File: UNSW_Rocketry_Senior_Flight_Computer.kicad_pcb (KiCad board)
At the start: 2 copper layers, 14 parts, among them U1 STM32L452RETx, U2 MS5611-01BA, U3 MS5611-01BA, U4 LIS3DH

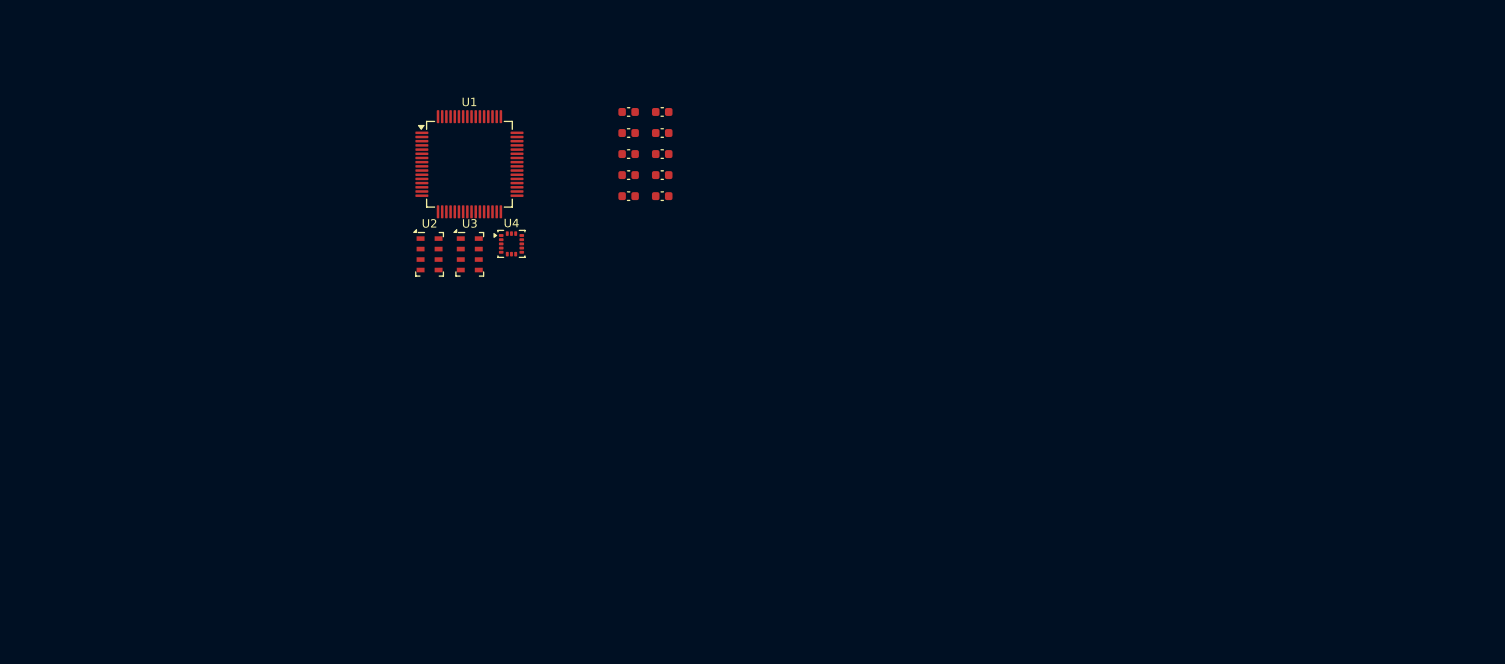
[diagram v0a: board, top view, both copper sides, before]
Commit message: feat: BCB Start ( power & pyro done)
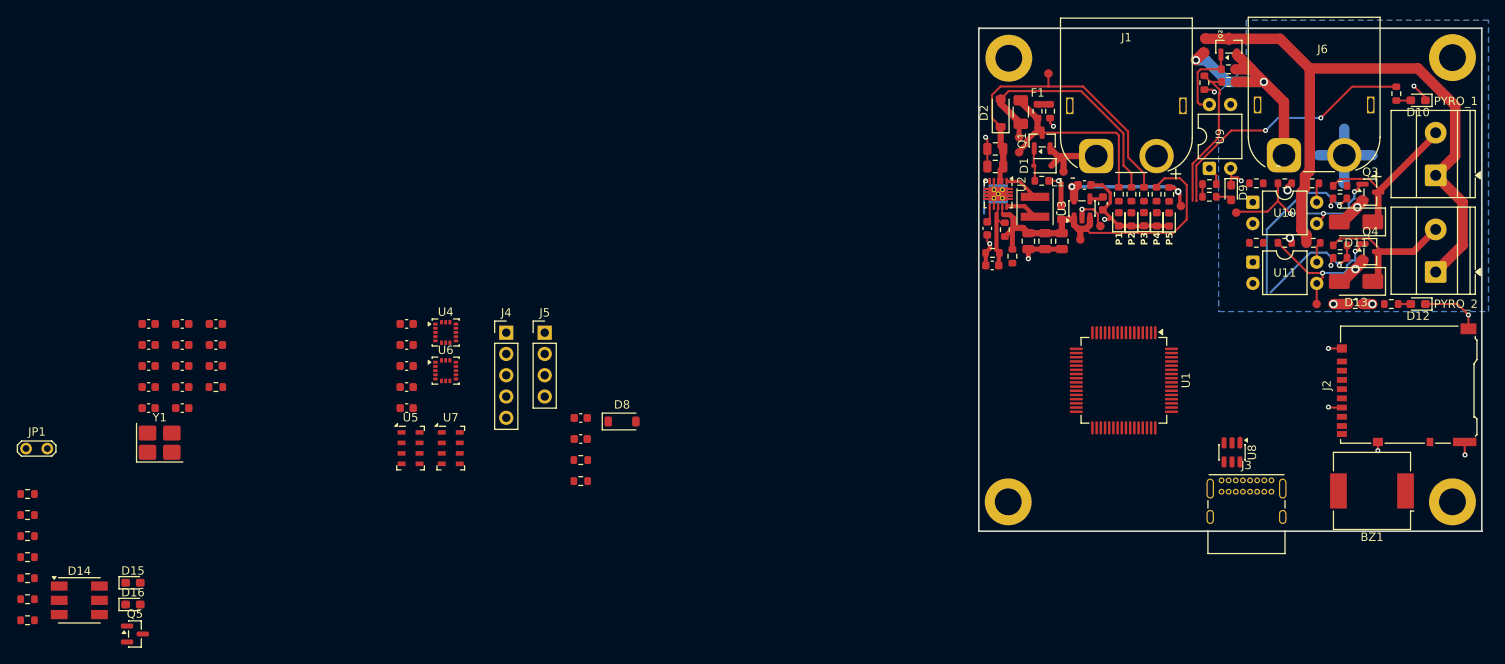
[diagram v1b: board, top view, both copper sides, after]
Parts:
- added BZ1: Buzzer, Buzzer_Beeper:Buzzer_CUI_CPT-9019S-SMT, F.Cu at (207.4, 114.7)
- added C11: 0.1uF, PCM_SparkFun-Capacitor:C_0603_1608Metric, F.Cu at (69.5, 94.8)
- added C12: 4.7uF, PCM_SparkFun-Capacitor:C_0603_1608Metric, F.Cu at (69.5, 97.3)
- added C13: 0.1uF, PCM_SparkFun-Capacitor:C_0603_1608Metric, F.Cu at (69.5, 99.8)
- added C14: 10uF, PCM_SparkFun-Capacitor:C_0805_2012Metric, F.Cu at (162.5, 73.9)
- added C15: 10uF, PCM_SparkFun-Capacitor:C_0805_2012Metric, F.Cu at (162.5, 76.0)
- added C16: 22uF, PCM_SparkFun-Capacitor:C_0805_2012Metric, F.Cu at (166.4, 84.9)
- added C17: 0.1uF, PCM_SparkFun-Capacitor:C_0603_1608Metric, F.Cu at (161.5, 83.4)
- added C18: 22uF, PCM_SparkFun-Capacitor:C_0805_2012Metric, F.Cu at (168.4, 84.9)
- added C19: 10pF, PCM_SparkFun-Capacitor:C_0603_1608Metric, F.Cu at (162.1, 87.8)
- added C20: 22uF, PCM_SparkFun-Capacitor:C_0805_2012Metric, F.Cu at (170.4, 84.9)
- added C21: 1.0uF, PCM_SparkFun-Capacitor:C_0603_1608Metric, F.Cu at (170.3, 81.5)
- added C22: 1.0uF, PCM_SparkFun-Capacitor:C_0603_1608Metric, F.Cu at (173.1, 78.2)
- added C23: 10nF, PCM_SparkFun-Capacitor:C_0603_1608Metric, F.Cu at (175.3, 80.4)
- added C24: 0.1uF, PCM_SparkFun-Capacitor:C_0603_1608Metric, F.Cu at (92.2, 94.8)
- added C25: 0.1uF, PCM_SparkFun-Capacitor:C_0603_1608Metric, F.Cu at (92.2, 97.3)
- added C26: 0.1uF, PCM_SparkFun-Capacitor:C_0603_1608Metric, F.Cu at (92.2, 99.8)
- added C27: 0.1uF, PCM_SparkFun-Capacitor:C_0603_1608Metric, F.Cu at (92.2, 102.3)
- added C28: 0.1uF, PCM_SparkFun-Capacitor:C_0603_1608Metric, F.Cu at (92.2, 104.8)
- added C29: 1.0uF, PCM_SparkFun-Capacitor:C_0603_1608Metric, F.Cu at (113.0, 106.0)
- added C30: 0.1uF, PCM_SparkFun-Capacitor:C_0603_1608Metric, F.Cu at (113.0, 108.5)
- added D1: 5.1V, Diode_SMD:D_SOD-323, F.Cu at (168.1, 75.9)
- added D10: LED_YELLOW, LED_SMD:LED_0603_1608Metric_Pad1.05x0.95mm_HandSolder, F.Cu at (212.9, 68.1)
- added D11: SMAJ15A, Diode_SMD:D_SMA, F.Cu at (205.5, 82.6)
- added D12: LED_YELLOW, LED_SMD:LED_0603_1608Metric_Pad1.05x0.95mm_HandSolder, F.Cu at (212.9, 92.4)
- added D13: SMAJ15A, Diode_SMD:D_SMA, F.Cu at (205.5, 89.7)
- added D14: LED_RGB, LED_SMD:LED_RGB_5050-6, F.Cu at (53.2, 127.8)
- added D15: LED_RED, LED_SMD:LED_0603_1608Metric_Pad1.05x0.95mm_HandSolder, F.Cu at (59.6, 125.7)
- added D16: LED_GREEN, LED_SMD:LED_0603_1608Metric_Pad1.05x0.95mm_HandSolder, F.Cu at (59.6, 128.2)
- added D2: B5819W, Diode_SMD:D_SOD-123, F.Cu at (163.1, 69.6)
- added D3: Green, LED_SMD:LED_0603_1608Metric, F.Cu at (177.2, 82.3)
- added D4: Green, LED_SMD:LED_0603_1608Metric, F.Cu at (180.2, 82.3)
- added D5: Green, LED_SMD:LED_0603_1608Metric, F.Cu at (178.7, 82.3)
- added D6: Green, LED_SMD:LED_0603_1608Metric, F.Cu at (181.7, 82.3)
- added D7: Green, LED_SMD:LED_0603_1608Metric, F.Cu at (183.2, 82.3)
- added D8: B5819W, Diode_SMD:D_SOD-123, F.Cu at (117.9, 106.4)
- added D9: LED_RED, LED_SMD:LED_0603_1608Metric_Pad1.05x0.95mm_HandSolder, F.Cu at (190.6, 79.1)
- added F1: 1A, Fuse:Fuse_1206_3216Metric, F.Cu at (165.5, 69.5)
- added H1: MountingHole, MountingHole:MountingHole_3.2mm_M3_DIN965_Pad, F.Cu at (164.1, 63.1)
- added H2: MountingHole, MountingHole:MountingHole_3.2mm_M3_DIN965_Pad, F.Cu at (217.0, 63.0)
- added H3: MountingHole, MountingHole:MountingHole_3.2mm_M3_DIN965_Pad, F.Cu at (217.0, 116.0)
- added H4: MountingHole, MountingHole:MountingHole_3.2mm_M3_DIN965_Pad, F.Cu at (164.0, 116.0)
- added J1: BATT_XT60, Connector_AMASS:AMASS_XT60PW-M_1x02_P7.20mm_Horizontal, F.Cu at (174.5, 74.8)
- added J2: Micro_SD_Card_Det1, Connector_Card:microSD_HC_Hirose_DM3AT-SF-PEJM5, F.Cu at (211.5, 102.0)
- added J3: USB_C_Receptacle_USB2.0_16P, Connector_USB:USB_C_Receptacle_GCT_USB4085, F.Cu at (189.4, 113.4)
- added J4: SWD, Connector_PinHeader_2.54mm:PinHeader_1x05_P2.54mm_Vertical, F.Cu at (104.1, 95.8)
- added J5: Conn_01x04, Connector_PinHeader_2.54mm:PinHeader_1x04_P2.54mm_Vertical, F.Cu at (108.7, 95.8)
- added J6: PYRO_XT60, Connector_AMASS:AMASS_XT60PW-M_1x02_P7.20mm_Horizontal, F.Cu at (196.9, 74.7)
- added JP1: RESET_JMP, TestPoint:TestPoint_2Pads_Pitch2.54mm_Drill0.8mm, F.Cu at (46.8, 109.6)
- added L1: 1µH, Inductor_SMD:L_Coilcraft_XxL4020, F.Cu at (167.2, 80.8)
- added PYRO_1: J_PYRO1, TerminalBlock_Phoenix:TerminalBlock_Phoenix_MKDS-1,5-2-5.08_1x02_P5.08mm_Horizontal, F.Cu at (215.0, 77.0)
- added PYRO_2: J_PYRO2, TerminalBlock_Phoenix:TerminalBlock_Phoenix_MKDS-1,5-2-5.08_1x02_P5.08mm_Horizontal, F.Cu at (215.0, 88.6)
- added Q1: DMG2301L, Package_TO_SOT_SMD:SOT-23, F.Cu at (168.1, 72.9)
- added Q2: AO3401A, Package_TO_SOT_SMD:SOT-23, F.Cu at (190.3, 61.7)
- added Q3: AO3400A, Package_TO_SOT_SMD:SOT-23, F.Cu at (207.2, 79.0)
- added Q4: AO3400A, Package_TO_SOT_SMD:SOT-23, F.Cu at (207.2, 86.2)
- added Q5: AO3400A, Package_TO_SOT_SMD:SOT-23, F.Cu at (59.8, 131.8)
- added R1: 10k, PCM_SparkFun-Resistor:R_0603_1608Metric, F.Cu at (69.5, 102.3)
- added R10: 4.7k, PCM_SparkFun-Resistor:R_0603_1608Metric, F.Cu at (178.7, 79.3)
- added R11: 1k, PCM_SparkFun-Resistor:R_0603_1608Metric, F.Cu at (181.7, 79.3)
- added R12: 1k, PCM_SparkFun-Resistor:R_0603_1608Metric, F.Cu at (183.2, 79.3)
- added R13: 5.1k, PCM_SparkFun-Resistor:R_0603_1608Metric, F.Cu at (113.0, 111.0)
- added R14: 5.1k, PCM_SparkFun-Resistor:R_0603_1608Metric, F.Cu at (113.0, 113.5)
- added R15: 10k, PCM_SparkFun-Resistor:R_0603_1608Metric, F.Cu at (190.3, 65.9)
- added R16: 3.3k, PCM_SparkFun-Resistor:R_0603_1608Metric, F.Cu at (187.4, 66.0)
- added R17: 0, PCM_SparkFun-Resistor:R_0603_1608Metric, F.Cu at (205.4, 92.4)
- added R18: 330, PCM_SparkFun-Resistor:R_0603_1608Metric, F.Cu at (188.0, 78.1)
- added R19: 1k, PCM_SparkFun-Resistor:R_0603_1608Metric, F.Cu at (188.0, 79.6)
- added R2: 620k, PCM_SparkFun-Resistor:R_0603_1608Metric, F.Cu at (163.6, 83.5)
- added R20: 330, PCM_SparkFun-Resistor:R_0603_1608Metric, F.Cu at (193.6, 78.0)
- added R21: 100k, PCM_SparkFun-Resistor:R_0603_1608Metric, F.Cu at (190.3, 64.4)
- added R22: 10k, PCM_SparkFun-Resistor:R_0603_1608Metric, F.Cu at (200.2, 78.0)
- added R23: 10k, PCM_SparkFun-Resistor:R_0603_1608Metric, F.Cu at (197.0, 78.0)
- added R24: 1k, PCM_SparkFun-Resistor:R_0603_1608Metric, F.Cu at (210.3, 67.3)
- added R25: 10k, PCM_SparkFun-Resistor:R_0603_1608Metric, F.Cu at (203.6, 78.3)
- added R26: 3.3k, PCM_SparkFun-Resistor:R_0603_1608Metric, F.Cu at (203.6, 79.8)
- added R27: 330, PCM_SparkFun-Resistor:R_0603_1608Metric, F.Cu at (193.6, 85.1)
- added R28: 10k, PCM_SparkFun-Resistor:R_0603_1608Metric, F.Cu at (200.4, 85.1)
- added R29: 10k, PCM_SparkFun-Resistor:R_0603_1608Metric, F.Cu at (197.0, 85.1)
- added R3: 100k, PCM_SparkFun-Resistor:R_0603_1608Metric, F.Cu at (164.5, 86.7)
- added R30: 1k, PCM_SparkFun-Resistor:R_0603_1608Metric, F.Cu at (209.7, 92.4)
- added R31: 10k, PCM_SparkFun-Resistor:R_0603_1608Metric, F.Cu at (203.6, 85.4)
- added R32: 3.3k, PCM_SparkFun-Resistor:R_0603_1608Metric, F.Cu at (203.6, 86.9)
- added R33: 100, PCM_SparkFun-Resistor:R_0603_1608Metric, F.Cu at (47.0, 115.1)
- added R34: 100, PCM_SparkFun-Resistor:R_0603_1608Metric, F.Cu at (47.0, 117.6)
- added R35: 100, PCM_SparkFun-Resistor:R_0603_1608Metric, F.Cu at (47.0, 120.1)
- added R36: 150, PCM_SparkFun-Resistor:R_0603_1608Metric, F.Cu at (47.0, 122.6)
- added R37: 10k, PCM_SparkFun-Resistor:R_0603_1608Metric, F.Cu at (47.0, 125.1)
- added R38: 1k, PCM_SparkFun-Resistor:R_0603_1608Metric, F.Cu at (47.0, 127.6)
- added R39: 1k, PCM_SparkFun-Resistor:R_0603_1608Metric, F.Cu at (47.0, 130.1)
- added R4: 100k, PCM_SparkFun-Resistor:R_0603_1608Metric, F.Cu at (162.1, 86.3)
- added R5: 100k, PCM_SparkFun-Resistor:R_0603_1608Metric, F.Cu at (168.0, 77.7)
- added R6: 10k, PCM_SparkFun-Resistor:R_0603_1608Metric, F.Cu at (169.0, 69.4)
- added R7: 33k, PCM_SparkFun-Resistor:R_0603_1608Metric, F.Cu at (167.5, 69.4)
- added R8: 4.7k, PCM_SparkFun-Resistor:R_0603_1608Metric, F.Cu at (177.2, 79.3)
- added R9: 4.7k, PCM_SparkFun-Resistor:R_0603_1608Metric, F.Cu at (180.2, 79.3)
- added TP1: 1.0mm, PCM_SparkFun-Connector:TestPoint-1.0mm, F.Cu at (170.6, 76.6)
- added TP10: 1.0mm, PCM_SparkFun-Connector:TestPoint-1.0mm, F.Cu at (191.2, 81.5)
- added TP12: 1.0mm, PCM_SparkFun-Connector:TestPoint-1.0mm, F.Cu at (200.8, 92.4)
- added TP2: 1.0mm, PCM_SparkFun-Connector:TestPoint-1.0mm, F.Cu at (172.6, 84.7)
- added TP3: 1.0mm, PCM_SparkFun-Connector:TestPoint-1.0mm, F.Cu at (165.3, 74.3)
- added TP4: 1.0mm, PCM_SparkFun-Connector:TestPoint-1.0mm, F.Cu at (175.0, 83.1)
- added TP5: 1.0mm, PCM_SparkFun-Connector:TestPoint-1.0mm, F.Cu at (184.6, 80.7)
- added TP6: 1.0mm, PCM_SparkFun-Connector:TestPoint-1.0mm, F.Cu at (165.3, 72.5)
- added TP7: 1.0mm, PCM_SparkFun-Connector:TestPoint-1.0mm, F.Cu at (168.8, 64.9)
- added TP8: 1.0mm, PCM_SparkFun-Connector:TestPoint-1.0mm, F.Cu at (187.4, 62.4)
- added TP9: 1.0mm, PCM_SparkFun-Connector:TestPoint-1.0mm, F.Cu at (187.5, 60.7)
- added U10: PC817, Package_DIP:DIP-4_W7.62mm, F.Cu at (193.2, 80.3)
- added U11: PC817, Package_DIP:DIP-4_W7.62mm, F.Cu at (193.2, 87.4)
- added U5: MS5611 #1, Package_LGA:LGA-8_3x5mm_P1.25mm, F.Cu at (92.7, 109.6)
- added U6: LIS3DH, Package_LGA:LGA-16_3x3mm_P0.5mm_LayoutBorder3x5y, F.Cu at (96.9, 100.3)
- added U7: MS5611 #2, Package_LGA:LGA-8_3x5mm_P1.25mm, F.Cu at (97.5, 109.6)
- added U8: USBLC6-2SC6, Package_TO_SOT_SMD:SOT-23-6, F.Cu at (190.7, 110.1)
- added U9: PC817, Package_DIP:DIP-4_W7.62mm, F.Cu at (188.0, 76.2)
- added Y1: 8MHz, Crystal:Crystal_SMD_3225-4Pin_3.2x2.5mm_HandSoldering, F.Cu at (62.8, 108.9)
- C1, C2: value 0.1uF -> 27pF
- C4: value 4.7uF -> 1.0uF
- C5: value 1.0uF -> 0.1uF
- C6: value 10nF -> 0.1uF
- C7: value 0.1uF -> 10nF
- U2: value MS5611-01BA -> TPS63060; footprint Package_LGA:LGA-8_3x5mm_P1.25mm -> Package_SON:Texas_S-PWSON-N10_ThermalVias
- U3: value MS5611-01BA -> SPX3819M5-L-3-3; footprint Package_LGA:LGA-8_3x5mm_P1.25mm -> Package_TO_SOT_SMD:SOT-23-5
- U4: value LIS3DH -> H3LIS331DL
- moved U1 82.2 mm to (177.8, 101.5), turned to -90 degrees
- moved U3 73.2 mm to (172.8, 81.0), turned to 90 degrees
- moved U2 68.2 mm to (162.8, 79.3), turned to -90 degrees
- moved C1 62.6 mm to (61.5, 94.8)
- moved C4 62.6 mm to (61.5, 102.3)
- moved C2 62.6 mm to (61.5, 97.3)
- moved C3 62.6 mm to (61.5, 99.8)
- moved C5 62.6 mm to (61.5, 104.8)
- moved C10 62.6 mm to (65.5, 104.8)
- moved C6 62.6 mm to (65.5, 94.8)
- moved C7 62.6 mm to (65.5, 97.3)
- moved C8 62.6 mm to (65.5, 99.8)
- moved C9 62.6 mm to (65.5, 102.3)
- moved U4 13.2 mm to (96.9, 95.8)
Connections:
- C1 pad 1: GND -> Net-(U1-PH1)
- C1 pad 2: +3.3V -> GND
- C10 pad 1: +3.3V -> GND
- C10 pad 2: GND -> +3.3V
- C2 pad 2: +3.3V -> Net-(U1-PH0)
- C3 pad 2: +3.3V -> NRST
- C6 pad 1: GND -> +3.3V
- C6 pad 2: +3.3V -> GND
- C8 pad 1: +3.3V -> GND
- C8 pad 2: GND -> +3.3V
- C9 pad 1: GND -> +3.3V
- C9 pad 2: +3.3V -> GND
- U1 pad 10: unconnected-(U1-PC2-Pad10) -> INT2_LIS3DH
- U1 pad 11: unconnected-(U1-PC3-Pad11) -> SD_CD
- U1 pad 14: unconnected-(U1-PA0-Pad14) -> PYRO1_CONT
- U1 pad 15: unconnected-(U1-PA1-Pad15) -> PYRO2_CONT
- U1 pad 16: unconnected-(U1-PA2-Pad16) -> UART_TX
- U1 pad 17: unconnected-(U1-PA3-Pad17) -> UART_RX
- U1 pad 20: unconnected-(U1-PA4-Pad20) -> PYRO_BATT_SENSE
- U1 pad 21: unconnected-(U1-PA5-Pad21) -> SPI1_SCK
- U1 pad 22: unconnected-(U1-PA6-Pad22) -> SPI1_MISO
- U1 pad 23: unconnected-(U1-PA7-Pad23) -> SPI1_MOSI
- U1 pad 24: unconnected-(U1-PC4-Pad24) -> VBAT_SENSE
- U1 pad 26: unconnected-(U1-PB0-Pad26) -> CS_H3LIS
- U1 pad 27: unconnected-(U1-PB1-Pad27) -> CS_LIS3DH
- U1 pad 28: unconnected-(U1-PB2-Pad28) -> CS_MS5611_1
- U1 pad 29: unconnected-(U1-PB10-Pad29) -> PYRO1_CONT_LED
- U1 pad 30: unconnected-(U1-PB11-Pad30) -> PYRO2_CONT_LED
- U1 pad 33: unconnected-(U1-PB12-Pad33) -> CS_MS5611_2
- U1 pad 34: unconnected-(U1-PB13-Pad34) -> PYRO_ARM
- U1 pad 35: unconnected-(U1-PB14-Pad35) -> PYRO1_GATE
- U1 pad 36: unconnected-(U1-PB15-Pad36) -> PYRO2_GATE
- U1 pad 39: unconnected-(U1-PC8-Pad39) -> SDMMC_D0
- U1 pad 40: unconnected-(U1-PC9-Pad40) -> SDMMC_D1
- U1 pad 41: unconnected-(U1-PA8-Pad41) -> RGB_R
- U1 pad 42: unconnected-(U1-PA9-Pad42) -> RGB_G
- U1 pad 43: unconnected-(U1-PA10-Pad43) -> RGB_B
- U1 pad 44: unconnected-(U1-PA11-Pad44) -> USB_N
- U1 pad 45: unconnected-(U1-PA12-Pad45) -> USB_P
- U1 pad 46: unconnected-(U1-PA13-Pad46) -> SWDIO
- U1 pad 49: unconnected-(U1-PA14-Pad49) -> SWCLK
- U1 pad 5: unconnected-(U1-PH0-Pad5) -> Net-(U1-PH0)
- U1 pad 51: unconnected-(U1-PC10-Pad51) -> SDMMC_D2
- U1 pad 52: unconnected-(U1-PC11-Pad52) -> SDMMC_D3
- U1 pad 53: unconnected-(U1-PC12-Pad53) -> SDMMC_CLK
- U1 pad 54: unconnected-(U1-PD2-Pad54) -> SDMMC_CMD
- U1 pad 58: unconnected-(U1-PB6-Pad58) -> LED_HEARTBEAT
- U1 pad 59: unconnected-(U1-PB7-Pad59) -> LED_ERROR
- U1 pad 6: unconnected-(U1-PH1-Pad6) -> Net-(U1-PH1)
- U1 pad 60: unconnected-(U1-PH3-Pad60) -> Net-(U1-PH3)
- U1 pad 61: unconnected-(U1-PB8-Pad61) -> PG_BUCKBOOST
- U1 pad 62: unconnected-(U1-PB9-Pad62) -> BUZZER
- U1 pad 7: unconnected-(U1-NRST-Pad7) -> NRST
- U1 pad 8: unconnected-(U1-PC0-Pad8) -> INT1_H3LIS
- U1 pad 9: unconnected-(U1-PC1-Pad9) -> INT1_LIS3DH
- U2 pad 1: unconnected-(U2-VDD-Pad1) -> Net-(U2-L1)
- U2 pad 2: unconnected-(U2-PS-Pad2) -> VBAT_FUSED
- U2 pad 3: unconnected-(U2-GND-Pad3) -> VBAT_FUSED
- U2 pad 4: Net-(U2-CSB-Pad4) -> GND
- U2 pad 5: Net-(U2-CSB-Pad4) -> PG_BUCKBOOST
- U2 pad 6: unconnected-(U2-SDO-Pad6) -> Net-(U2-VAUX)
- U2 pad 7: unconnected-(U2-SDI/SDA-Pad7) -> GND
- U2 pad 8: unconnected-(U2-SCLK-Pad8) -> Net-(U2-FB)
- U3 pad 1: unconnected-(U3-VDD-Pad1) -> +3.6V
- U3 pad 2: unconnected-(U3-PS-Pad2) -> GND
- U3 pad 3: unconnected-(U3-GND-Pad3) -> +3.6V
- U3 pad 4: Net-(U3-CSB-Pad4) -> Net-(U3-BP)
- U3 pad 5: Net-(U3-CSB-Pad4) -> +3.3V
- U4 pad 1: unconnected-(U4-VDD_IO-Pad1) -> +3.3V
- U4 pad 10: Net-(U4-GND-Pad10) -> GND
- U4 pad 11: unconnected-(U4-INT1-Pad11) -> INT1_H3LIS
- U4 pad 12: Net-(U4-GND-Pad10) -> GND
- U4 pad 13: unconnected-(U4-ADC3-Pad13) -> GND
- U4 pad 14: unconnected-(U4-VDD-Pad14) -> +3.3V
- U4 pad 15: unconnected-(U4-ADC2-Pad15) -> +3.3V
- U4 pad 16: unconnected-(U4-ADC1-Pad16) -> GND
- U4 pad 4: unconnected-(U4-SPC-Pad4) -> SPI1_SCK
- U4 pad 5: Net-(U4-GND-Pad10) -> GND
- U4 pad 6: unconnected-(U4-SDI-Pad6) -> SPI1_MOSI
- U4 pad 7: unconnected-(U4-SDO-Pad7) -> SPI1_MISO
- U4 pad 8: unconnected-(U4-CS-Pad8) -> CS_H3LIS
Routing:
- net PYRO_BATT: track 0.00 -> 78.1 mm
- net GND: track 0.00 -> 64.8 mm, vias 0 -> 18
- net +3.6V: track 0.00 -> 43.7 mm
- net VBAT_FUSED: track 0.00 -> 38.9 mm
- net PYRO1_CONT_LED: track 0.00 -> 32.0 mm, vias 0 -> 2
- net PYRO_BATT_RAW: track 0.00 -> 30.2 mm, vias 0 -> 2
- net /Power/VBAT_POLY_STATUS: track 0.00 -> 29.8 mm
- net PYRO_GND: track 0.00 -> 26.6 mm, vias 0 -> 5
- net VBAT_PROT: track 0.00 -> 24.5 mm
- net Net-(Q3-G): track 0.00 -> 22.5 mm, vias 0 -> 3
- net Net-(D11-A1): track 0.00 -> 20.4 mm
- net PYRO1_CONT: track 0.00 -> 20.1 mm, vias 0 -> 1
- net PYRO_BATT_SENSE: track 0.00 -> 18.5 mm
- net Net-(D13-A1): track 0.00 -> 18.4 mm
- net +3.3V: track 0.00 -> 18.1 mm, vias 0 -> 2
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- added copper zone on In1.Cu, net GND
- added copper zone on B.Cu, net PYRO_GND
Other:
- board outline added: 60 x 60 mm
- copper layers 2 -> 4
- board text added: "P1"
- board text added: "P2"
- board text added: "P3"
- board text added: "P4"
- board text added: "P5"
